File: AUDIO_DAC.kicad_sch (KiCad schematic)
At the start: 37 parts, among them J5 Audio out, U10 MCP1541-TT, U11 MCP4922-ESL, U13 LMV358, U8 LMV324, U9 MCP4922-ESL

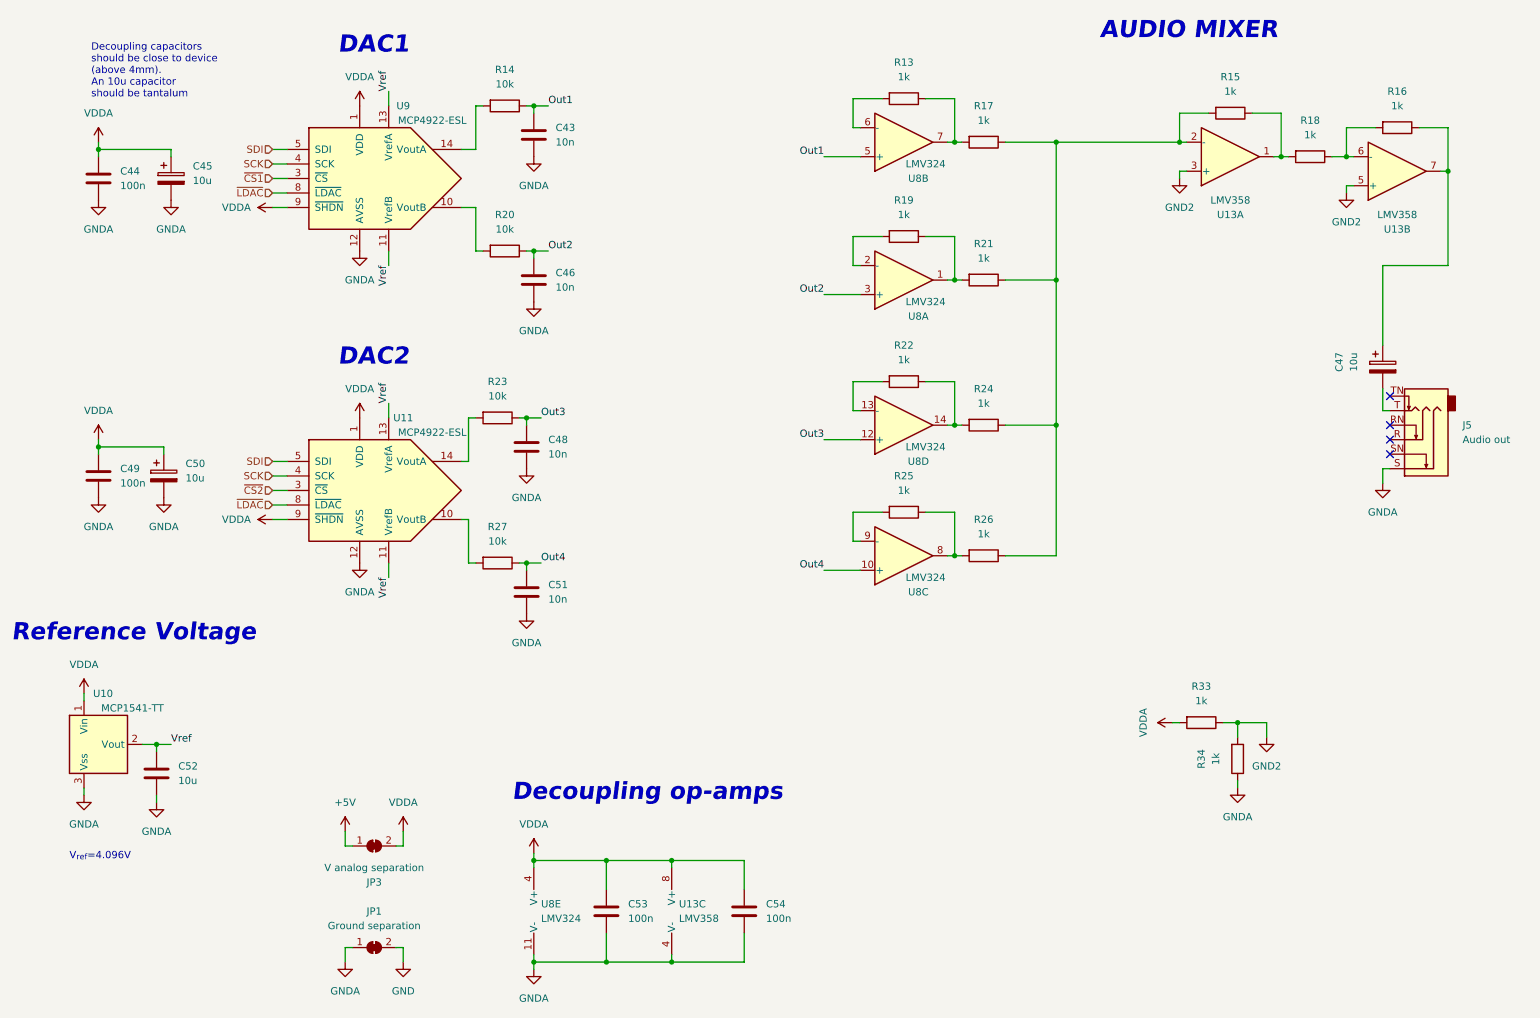
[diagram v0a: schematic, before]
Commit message: fix: Remove second DAC
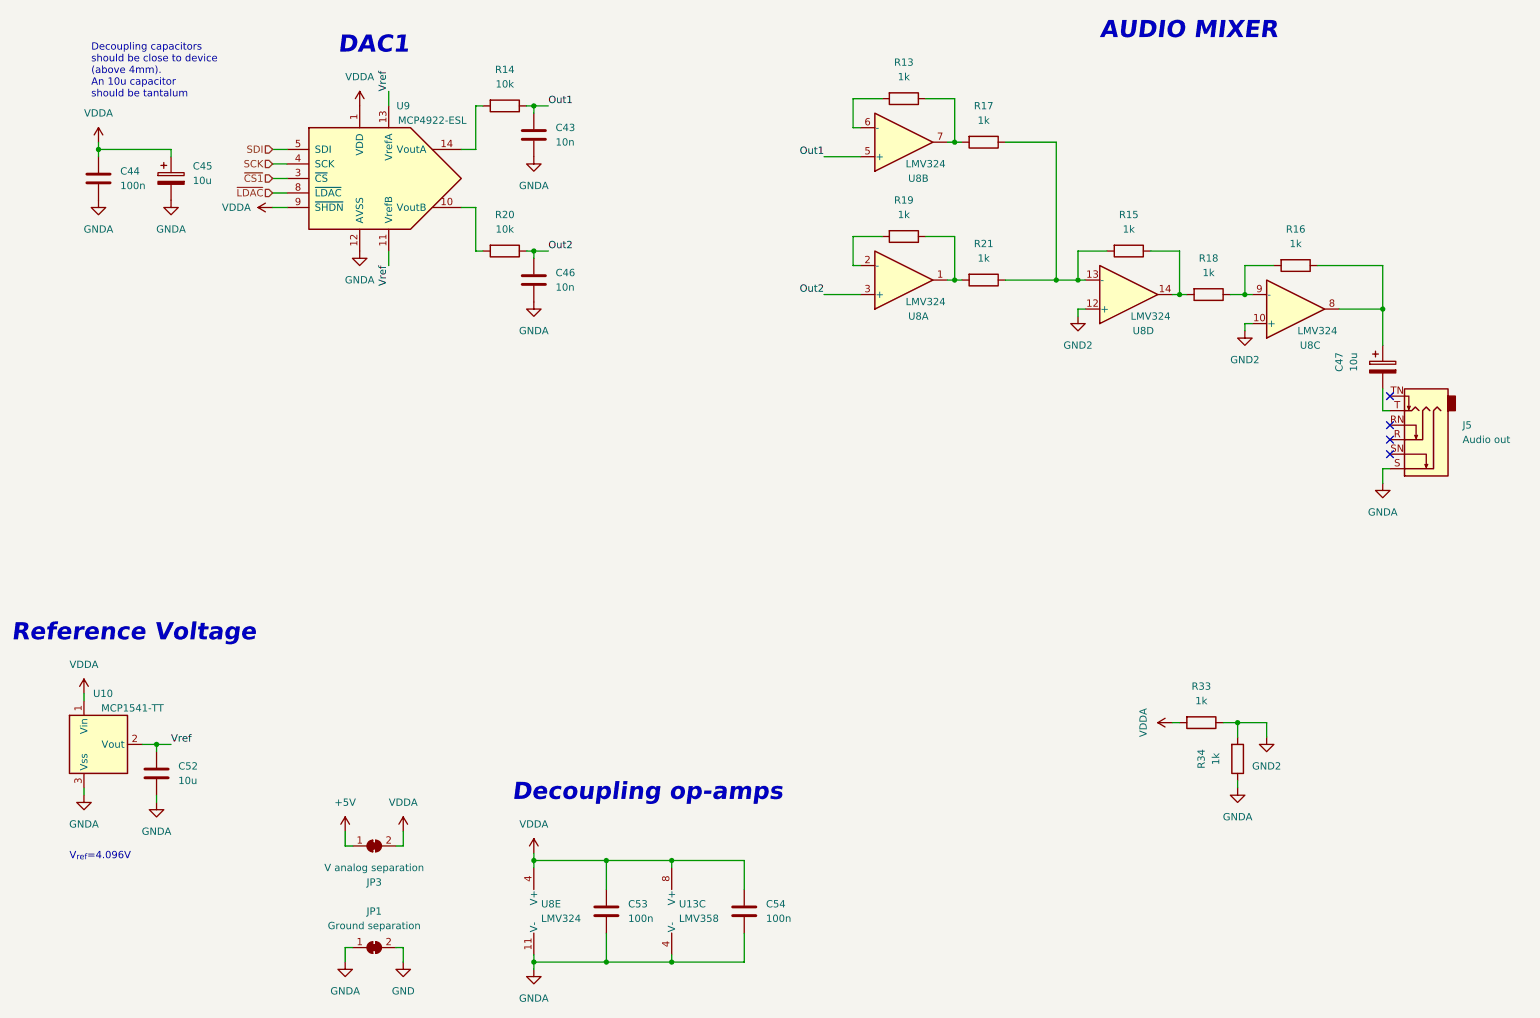
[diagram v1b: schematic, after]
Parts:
- removed C48, C51: 10n, Capacitor_SMD:C_0603_1608Metric_Pad1.08x0.95mm_HandSolder, symbol Device:C
- removed C49: 100n, Capacitor_SMD:C_0603_1608Metric_Pad1.08x0.95mm_HandSolder, symbol Device:C
- removed C50: 10u, Capacitor_SMD:C_1206_3216Metric_Pad1.33x1.80mm_HandSolder, symbol Device:C_Polarized
- removed R22, R24, R25, R26: 1k, Resistor_SMD:R_0603_1608Metric_Pad0.98x0.95mm_HandSolder, symbol Device:R
- removed R23, R27: 10k, Resistor_SMD:R_0603_1608Metric_Pad0.98x0.95mm_HandSolder, symbol Device:R
- removed U11: MCP4922-ESL, Package_SO:SOIC-14_3.9x8.7mm_P1.27mm, symbol Analog_DAC:MCP4922-ESL
- removed unit 2 of U13
- removed unit 1 of U13
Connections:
- net Out3 is gone; now on net GND2: U8.12 (+)
- net Out4 is gone; now on net GND2: U8.10 (+)
- net at R16.2, R18.1: now also U8.9 (-)
- net at C47.1, R16.1: now also U8.8
- net at R15.2, R17.1, R21.1: now also U8.13 (-)
- net at U8.14: now also R15.1, R18.2
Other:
- note removed: "DAC2"
- moved on the sheet: R15, R16, R18, U8C, U8D
